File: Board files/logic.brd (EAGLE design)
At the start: 44.5 x 57.1 mm, 22 parts, among them U1 LD1117, U2 LM2662, U3 LD1085V

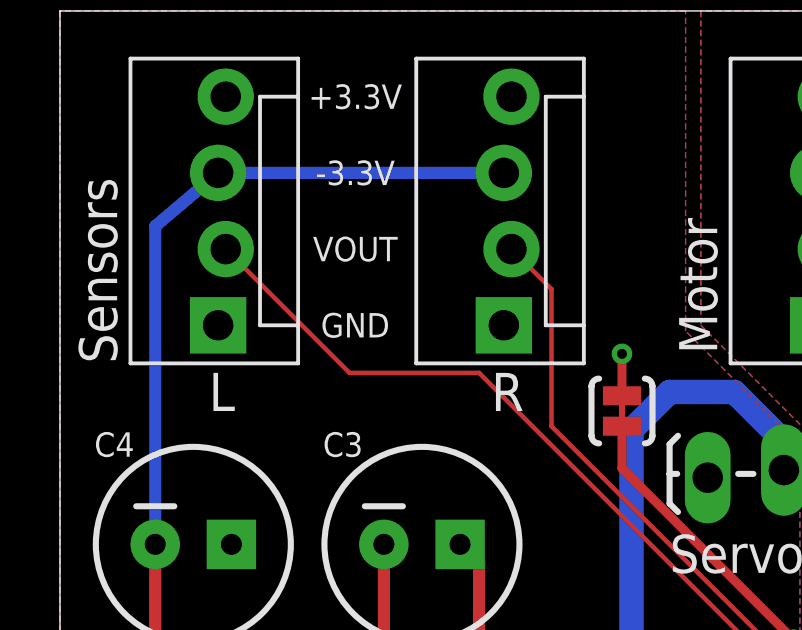
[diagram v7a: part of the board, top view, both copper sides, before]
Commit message: Modified a trace, sending the boards out to manufacture
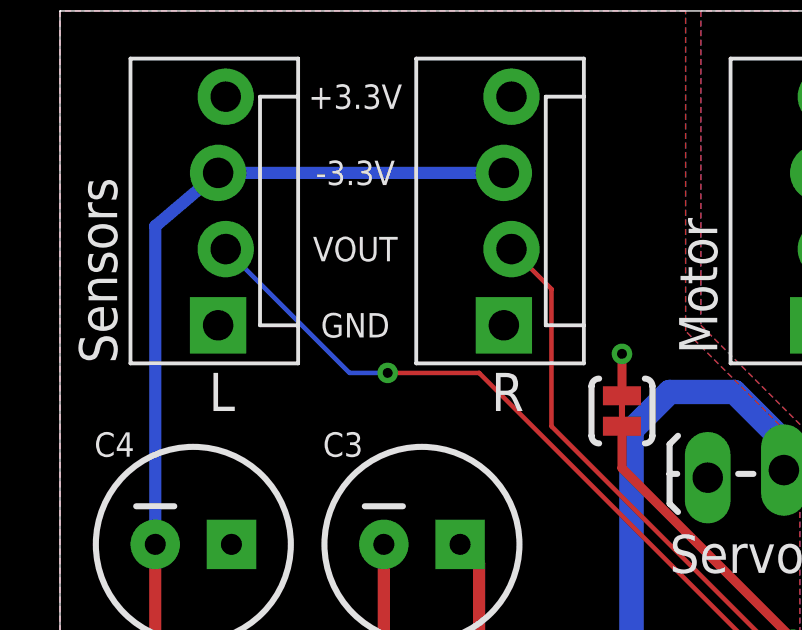
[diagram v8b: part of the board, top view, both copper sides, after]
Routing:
- net N$13: vias 0 -> 1
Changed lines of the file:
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@@
 <wire x1="25.019" y1="32.131" x2="25.019" y2="34.036" width="0.1524" layer="1"/>
 <wire x1="25.019" y1="34.036" x2="13.97" y2="45.085" width="0.1524" layer="1"/>
-<wire x1="13.97" y1="45.085" x2="9.652" y2="45.085" width="0.1524" layer="1"/>
-<wire x1="9.652" y1="45.085" x2="5.5245" y2="49.2125" width="0.1524" layer="1"/>
+<wire x1="13.97" y1="45.085" x2="10.922" y2="45.085" width="0.1524" layer="1"/>
+<via x="10.922" y="45.085" extent="1-16" drill="0.3302"/>
+<wire x1="10.922" y1="45.085" x2="9.652" y2="45.085" width="0.1524" layer="16"/>
+<wire x1="9.652" y1="45.085" x2="5.5245" y2="49.2125" width="0.1524" layer="16"/>
 </signal>
 <signal name="N$12">
